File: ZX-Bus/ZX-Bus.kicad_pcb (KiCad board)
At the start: 2 copper layers, 177 x 146 mm, 51 parts, among them J1 DIP-40 Pins, J2 PLS-3, J3 PLS-6, J4 Power, J5 Main board power, J6 12V, J7 5V, J8 Reset, J9 PLS-2R, U1 Z84C00xxP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

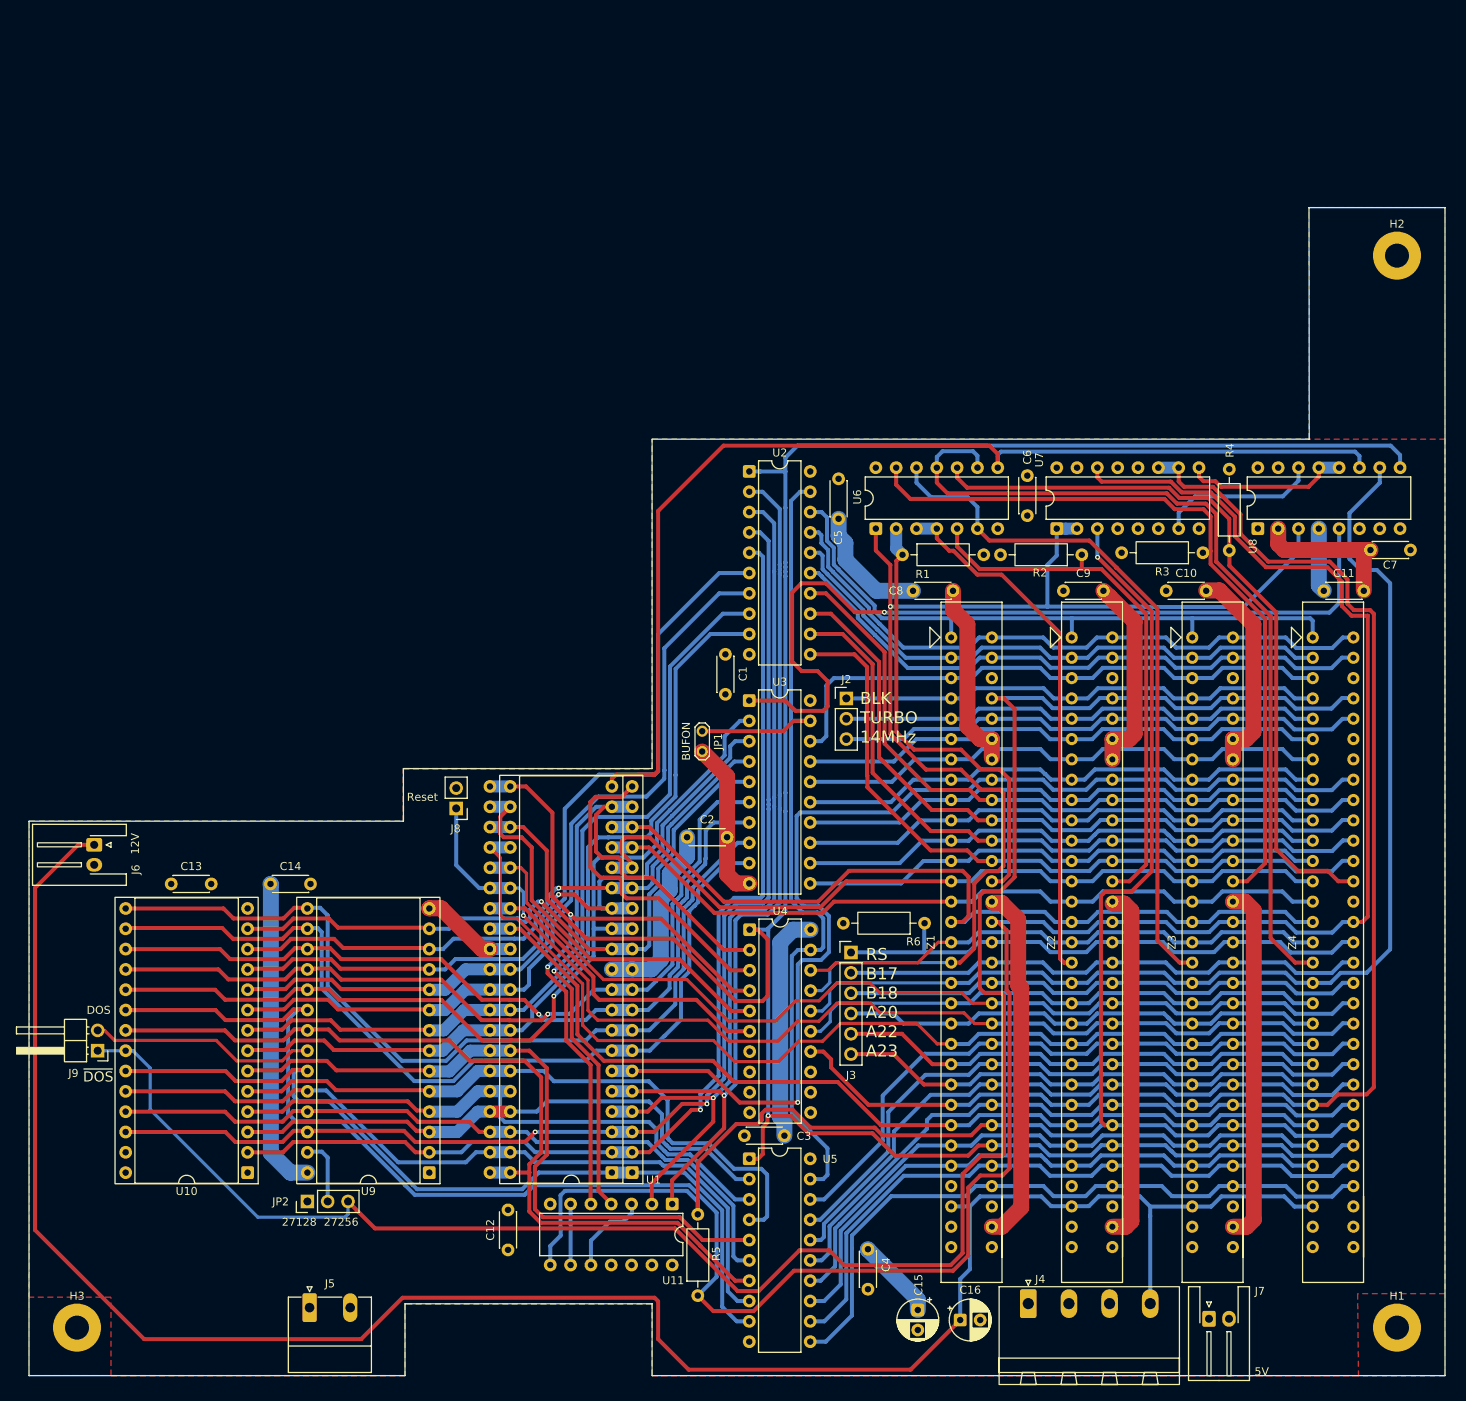
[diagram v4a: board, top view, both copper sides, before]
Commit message: ZX-Bus: Fix holes position and borders
According to measurements and fit test with the mockup
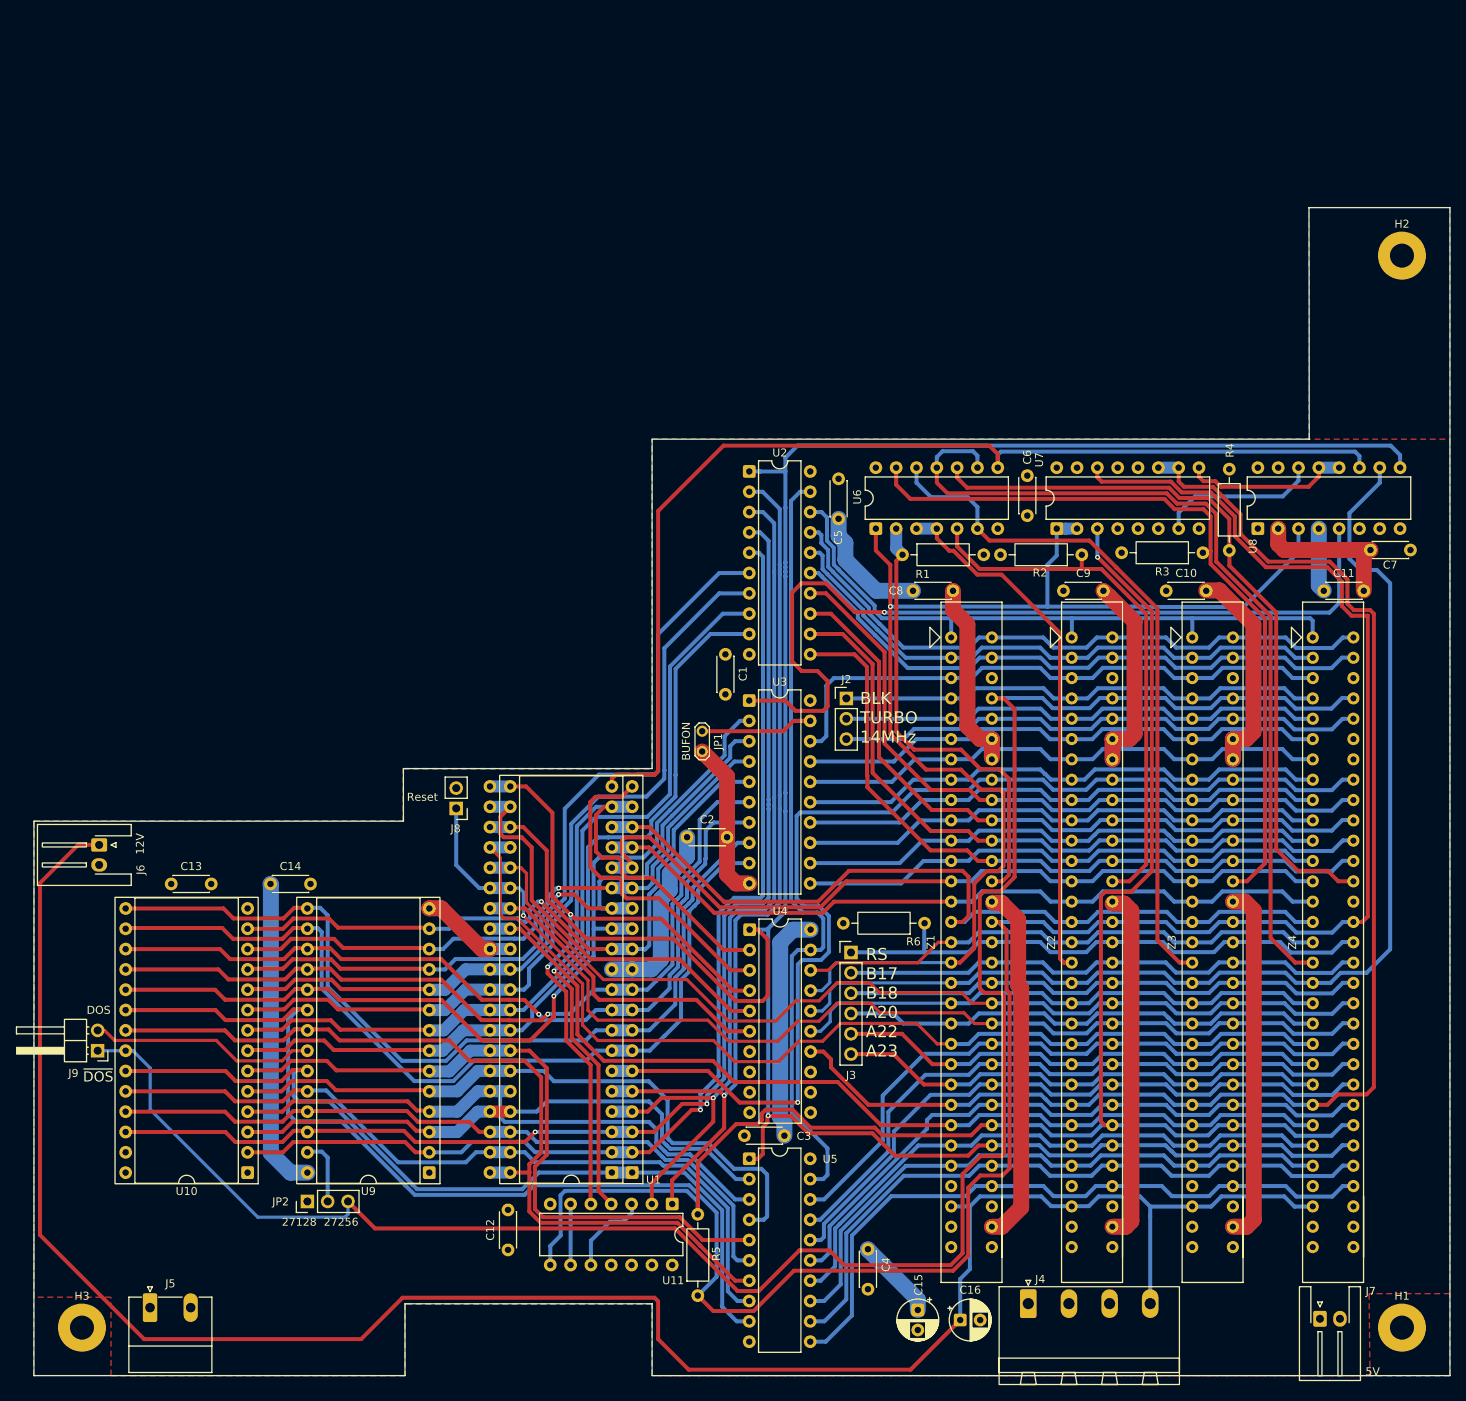
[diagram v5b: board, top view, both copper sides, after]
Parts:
- moved J5 19.9 mm to (30.3, 192.3)
- moved J7 13.9 mm to (176.5, 193.7)
- moved J6 0.62 mm to (23.9, 134.5)
- moved H1 0.62 mm to (186.8, 194.8)
- moved H2 0.62 mm to (186.8, 60.8)
- moved H3 0.62 mm to (21.8, 194.8)
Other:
- outline, holes or cut-outs redrawn
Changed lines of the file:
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@@
 		(capping no)
 		(filling no)
-		(grid_origin 186.1516 194.80155)
+		(grid_origin 72.7716 175.41675)
 		(pcbplotparams
 			(layerselection 0x00000000_00000000_55555555_5755f5ff)
@@
 	(footprint "MountingHole:MountingHole_3mm_Pad"
 		(layer "F.Cu")
-		(at 186.1516 194.80155)
+		(at 186.7716 194.80155)
 		(descr "Mounting Hole 3mm, generated by kicad-footprint-generator mountinghole.py")
 		(tags "mountinghole")
@@
 	(footprint "Connector_JST:JST_XH_S2B-XH-A-1_1x02_P2.50mm_Horizontal"
 		(layer "F.Cu")
-		(at 162.6516 193.70155)
+		(at 176.5216 193.70155)
 		(descr "JST XH series connector, S2B-XH-A-1 (http://www.jst-mfg.com/product/pdf/eng/eXH.pdf)")
 		(tags "connector JST XH horizontal")
@@
 	(footprint "Connector_JST:JST_XH_S2B-XH-A-1_1x02_P2.50mm_Horizontal"
 		(layer "F.Cu")
-		(at 23.3016 134.45155 -90)
+		(at 23.9216 134.46675 -90)
 		(descr "JST XH series connector, S2B-XH-A-1 (http://www.jst-mfg.com/product/pdf/eng/eXH.pdf)")
 		(tags "connector JST XH horizontal")
@@
 	(footprint "MountingHole:MountingHole_3mm_Pad"
 		(layer "F.Cu")
-		(at 21.1516 194.80155)
+		(at 21.7716 194.80155)
 		(descr "Mounting Hole 3mm, generated by kicad-footprint-generator mountinghole.py")
 		(tags "mountinghole")
@@
 		)
 		(property "Value" "MountingHole 3mm"
-			(at 2 4 0)
+			(at -2 -5.3848 0)
 			(layer "F.Fab")
 			(effects
@@
 	(footprint "Connector_Phoenix_MC_HighVoltage:PhoenixContact_MC_1,5_2-G-5.08_1x02_P5.08mm_Horizontal"
 		(layer "F.Cu")
-		(at 50.2216 192.30155)
+		(at 30.2816 192.30155)
 		(descr "Generic Phoenix Contact connector footprint for: MC_1,5/2-G-5.08; number of pins: 02; pin pitch: 5.08mm; Angled || order number: 1836189 8A 320V")
 		(tags "phoenix_contact connector MC_01x02_G_5.08mm")
@@
 	(footprint "MountingHole:MountingHole_3mm_Pad"
 		(layer "F.Cu")
-		(at 186.1516 60.80155)
+		(at 186.7716 60.80155)
 		(descr "Mounting Hole 3mm, generated by kicad-footprint-generator mountinghole.py")
 		(tags "mountinghole")
@@
 	)
 	(gr_line
-		(start 15.1516 131.50155)
+		(start 15.7716 131.50155)
 		(end 61.9516 131.50155)
 		(stroke
@@
 	)
 	(gr_line
-		(start 15.1516 200.80155)
-		(end 15.1516 131.50155)
+		(start 15.7716 200.80155)
+		(end 15.7716 131.50155)
 		(stroke
 			(width 0.05)
@@
 	(gr_line
 		(start 62.1516 200.80155)
-		(end 15.1516 200.80155)
+		(end 15.7716 200.80155)
 		(stroke
 			(width 0.05)
@@
 	(gr_line
 		(start 93.0408 200.80155)
-		(end 192.1516 200.80155)
+		(end 192.7716 200.80155)
 		(stroke
 			(width 0.05)
@@
 	)
 	(gr_line
-		(start 192.1516 54.80155)
+		(start 192.7716 54.80155)
 		(end 175.1516 54.80155)
 		(stroke
@@
 	)
 	(gr_line
-		(start 192.1516 200.80155)
-		(end 192.1516 54.80155)
+		(start 192.7716 200.80155)
+		(end 192.7716 54.80155)
 		(stroke
 			(width 0.05)
-			(type default)
+			(type solid)
 		)
 		(layer "Edge.Cuts")
@@
 		(layer "Dwgs.User")
 		(pts
-			(xy 21.1516 194.80155) (xy 21.1516 200.80155)
+			(xy 21.7716 194.80155) (xy 15.7716 200.80155)
 		)
 		(height -7)
@@
 		)
 		(gr_text "6"
-			(at 13.0016 197.80155 90)
+			(at 13.6216 197.80155 90)
 			(layer "Dwgs.User")
 			(effects
@@
 		(layer "Dwgs.User")
 		(pts
-			(xy 186.1516 194.80155) (xy 192.1516 200.80155)
+			(xy 186.7716 194.80155) (xy 192.7716 200.80155)
 		)
-		(height 13)
+		(height 16.990211)
 		(orientation 0)
 		(format
@@
 		)
 		(gr_text "6"
-			(at 189.1516 206.65155 0)
+			(at 189.7716 210.641761 0)
 			(layer "Dwgs.User")
 			(effects
@@
 		(layer "Dwgs.User")
 		(pts
-			(xy 21.1516 194.80155) (xy 15.1516 200.80155)
+			(xy 21.7716 194.80155) (xy 15.7716 200.80155)
 		)
-		(height 12.875784)
+		(height 16.990211)
 		(orientation 0)
 		(format
@@
 		)
 		(gr_text "6"
-			(at 18.1516 206.527334 0)
+			(at 18.7716 210.641761 0)
 			(layer "Dwgs.User")
 			(effects
@@
 		(layer "Dwgs.User")
 		(pts
-			(xy 186.1516 194.80155) (xy 192.1516 200.80155)
+			(xy 186.7716 194.80155) (xy 192.7716 200.80155)
 		)
 		(height 8)
@@
 		)
 		(gr_text "6"
-			(at 193.0016 197.80155 90)
+			(at 193.6216 197.80155 90)
 			(layer "Dwgs.User")
 			(effects
@@
 		(layer "Dwgs.User")
 		(pts
-			(xy 186.1516 194.80155) (xy 21.1516 195.80155)
+			(xy 186.7716 194.80155) (xy 21.7716 194.80155)
 		)
-		(height 12.875784)
+		(height 16.990211)
 		(orientation 0)
 		(format
@@
 		)
 		(gr_text "165"
-			(at 103.6516 206.527334 0)
+			(at 104.2716 210.641761 0)
 			(layer "Dwgs.User")
 			(effects
@@
 		(layer "Dwgs.User")
 		(pts
-			(xy 186.1516 194.80155) (xy 186.1516 60.80155)
+			(xy 186.7716 194.80155) (xy 186.7716 60.80155)
 		)
-		(height 8.064578)
+		(height 8.05)
 		(orientation 1)
 		(format
@@
 		)
 		(gr_text "134"
-			(at 193.066178 127.80155 90)
+			(at 193.6716 127.80155 90)
 			(layer "Dwgs.User")
 			(effects
@@
 		(layer "Dwgs.User")
 		(pts
-			(xy 186.1516 60.80155) (xy 192.1516 54.80155)
+			(xy 72.7716 175.41675) (xy 186.7716 194.80155)
+		)
+		(height 32.9848)
+		(orientation 0)
+		(format
+			(prefix "")
+			(suffix "")
+			(units 3)
+			(units_format 0)
+			(precision 4)
+			(suppress_zeroes yes)
+		)
+		(style
+			(thickness 0.1)
+			(arrow_length 1.27)
+			(text_position_mode 0)
+			(arrow_direction outward)
+			(extension_height 0.58642)
+			(extension_offset 0.5)
+			(keep_text_aligned yes)
+		)
+		(gr_text "114"
+			(at 129.7716 207.25155 0)
+			(layer "Dwgs.User")
+			(effects
+				(font
+					(size 1 1)
+					(thickness 0.15)
+				)
+			)
+		)
+	)
+	(dimension
+		(type orthogonal)
+		(layer "Dwgs.User")
+		(pts
+			(xy 186.7716 60.80155) (xy 192.7716 54.80155)
 		)
 		(height -10)
@@
 		)
 		(gr_text "6"
-			(at 189.1516 49.65155 0)
+			(at 189.7716 49.65155 0)
 			(layer "Dwgs.User")
 			(effects
@@
 		(layer "Dwgs.User")
 		(pts
-			(xy 186.1516 60.80155) (xy 192.1516 54.80155)
+			(xy 186.7716 60.80155) (xy 192.7716 54.80155)
 		)
-		(height 8)
+		(height 8.05)
 		(orientation 1)
 		(format
@@
 		)
 		(gr_text "6"
-			(at 193.0016 57.80155 90)
+			(at 193.6716 57.80155 90)
 			(layer "Dwgs.User")
 			(effects
@@
 	)
 	(segment
-		(start 29.53605 196.236)
-		(end 15.9016 182.60155)
+		(start 56.67169 196.236)
+		(end 29.53605 196.236)
 		(width 0.5)
 		(layer "F.Cu")
@@
 	)
 	(segment
-		(start 93.7908 196.24075)
-		(end 93.7908 191.50609)
+		(start 16.5216 183.22155)
+		(end 16.5216 139.23155)
 		(width 0.5)
 		(layer "F.Cu")
@@
 	)
 	(segment
-		(start 93.7908 191.50609)
-		(end 93.35146 191.06675)
+		(start 131.5516 193.85155)
+		(end 125.3516 200.05155)
 		(width 0.5)
 		(layer "F.Cu")
@@
 	)
 	(segment
-		(start 56.67169 196.236)
-		(end 29.53605 196.236)
+		(start 16.5216 139.23155)
+		(end 21.3016 134.45155)
 		(width 0.5)
 		(layer "F.Cu")
@@
 	)
 	(segment
-		(start 15.9016 182.60155)
-		(end 15.9016 139.85155)
+		(start 93.35146 191.06675)
+		(end 61.84094 191.06675)
 		(width 0.5)
 		(layer "F.Cu")
@@
 	)
 	(segment
-		(start 131.5516 193.85155)
-		(end 125.3516 200.05155)
+		(start 21.3016 134.45155)
+		(end 23.9064 134.45155)
 		(width 0.5)
 		(layer "F.Cu")
@@
 	)
 	(segment
-		(start 125.3516 200.05155)
-		(end 97.6016 200.05155)
+		(start 61.84094 191.06675)
+		(end 56.67169 196.236)
 		(width 0.5)
 		(layer "F.Cu")
@@
 	)
 	(segment
-		(start 93.35146 191.06675)
-		(end 61.84094 191.06675)
+		(start 93.7908 191.50609)
+		(end 93.35146 191.06675)
 		(width 0.5)
 		(layer "F.Cu")
@@
 	)
 	(segment
-		(start 15.9016 139.85155)
-		(end 21.3016 134.45155)
+		(start 93.7908 196.24075)
+		(end 93.7908 191.50609)
 		(width 0.5)
 		(layer "F.Cu")
@@
 	)
 	(segment
-		(start 61.84094 191.06675)
-		(end 56.67169 196.236)
+		(start 125.3516 200.05155)
+		(end 97.6016 200.05155)
 		(width 0.5)
 		(layer "F.Cu")
@@
 	)
 	(segment
-		(start 21.3016 134.45155)
-		(end 23.3016 134.45155)
+		(start 23.9064 134.45155)
+		(end 23.9216 134.46675)
+		(width 0.5)
+		(layer "F.Cu")
+		(net "+12V")
+	)
+	(segment
+		(start 29.53605 196.236)
+		(end 16.5216 183.22155)
 		(width 0.5)
 		(layer "F.Cu")
@@
 		(polygon
 			(pts
-				(xy 15.190556 131.50003) (xy 61.9516 131.50155) (xy 61.941728 124.92277) (xy 93.0408 124.911) (xy 93.0408 83.75155)
-				(xy 192.1516 83.75155) (xy 192.1516 190.55155) (xy 181.227469 190.55155) (xy 181.339258 200.836)
+				(xy 15.772568 131.499973) (xy 61.9516 131.50155) (xy 61.941728 124.92277) (xy 93.0408 124.911) (xy 93.0408 83.75155)
+				(xy 192.7516 83.75155) (xy 192.7516 190.55155) (xy 182.663567 190.55155) (xy 182.775357 200.836)
 				(xy 93.0408 200.836) (xy 93.044825 191.853058) (xy 62.164874 191.832924) (xy 62.155427 200.801604)
-				(xy 25.4016 200.80155) (xy 25.4016 191.00155) (xy 15.188622 191.005863)
+				(xy 25.4016 200.80155) (xy 25.4016 191.00155) (xy 15.770634 191.005698)
 			)
 		)
@@
 		(polygon
 			(pts
-				(xy 15.190498 131.474975) (xy 61.9516 131.50155) (xy 61.9516 124.93603) (xy 93.0408 124.936) (xy 93.0408 83.757367)
-				(xy 175.152668 83.751321) (xy 175.150536 54.80155) (xy 192.1516 54.80155) (xy 192.1516 200.811)
+				(xy 15.7905 131.475344) (xy 61.9516 131.50155) (xy 61.9516 124.93603) (xy 93.0408 124.936) (xy 93.0408 83.757367)
+				(xy 175.152668 83.751321) (xy 175.150536 54.80155) (xy 192.7716 54.80155) (xy 192.7716 200.811)
 				(xy 93.041369 200.811) (xy 93.048269 191.85167) (xy 62.151616 191.827834) (xy 62.151458 200.802078)
-				(xy 15.151099 200.801196)
+				(xy 15.7511 200.80118)
 			)
 		)
